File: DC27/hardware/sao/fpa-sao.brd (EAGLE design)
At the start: 160 x 100 mm, 45 parts, among them IC1 LDL112D33R, U1 ICE40UL1K-SWG16ITR1K, U2 MIC5504-1.2YM5-TR, U3 W25X20CLSNIG

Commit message: checking in sao changes
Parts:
- removed IC1: LDL112D33R, voltage-regulator:SOIC127P600X175-8N
- removed LED2, LED6, LED7, LED8: (no value), leds:LED3MM
- removed R10, R11, R5, R6, R7, R8, R9: (no value), passives:0805
- removed R4: 10 K, passives:0805
- removed U$12, U$13, U$14, U$15, U$16, U$17, U$18, U$19: APA1025050, leds:APA102_5050
- removed U1: ICE40UL1K-SWG16ITR1K, FPGA:BGA16N35P4X4_140X140X49N
- added C16: 15 pF, passives:C0805
- added C5: 0.1 uF, passives:C0805
- added J1: (no value), connector:1X06
- added J2: FPGA_PROG, connector:2X5_NOSILK
- added J3, J4: (no value), connector:1X18
- added LED1: (no value), leds:LED3MM
- added R2: 56 R, passives:1206
- added R3: 10 K, passives:0805
- added S1, S2: (no value), switches:SWITCH-SPDT_KIT
- added U$1: DC-27-SAO, defcon:3X2
- added U$10, U$6, U$7, U$8, U$9: APA1025050, leds:APA102_5050
- added U4: MIC5504-3.3YM5-TR, voltage-regulator:SOT23-5P95_280X145XL45X37N
- added U5: ICE5LP1K-SG48ITR, FPGA:QFN50P700X700X100-49N
- C10, C11, C12, C13: value 15 pF -> 0.1 uF
- C4: value 1 uF -> 0.1 uF
- moved R12 103.4 mm to (40.3, 89.0), turned to 180 degrees
- moved R13 99.1 mm to (29.2, 85.9), turned to 270 degrees
- moved U3 96.0 mm to (35.5, 85.6), turned to 180 degrees
- moved C15 95.2 mm to (24.6, 84.9)
- moved C4 70.5 mm to (-11.9, 2.45)
- moved C13 66.9 mm to (-32.9, 2.45)
- moved C12 56.1 mm to (-28.7, 2.45)
- moved LED3 52.0 mm to (39.8, 77.8), turned to 180 degrees
- moved C1 43.2 mm to (12.7, 97.8)
- moved LED4 42.8 mm to (39.8, 72.3), turned to 180 degrees
- moved C11 42.3 mm to (-24.5, 2.45)
- moved C2 41.6 mm to (15.9, 91.6), turned to 90 degrees
- moved LED5 32.2 mm to (40.1, 66.9), turned to 180 degrees
- moved C3 30.1 mm to (12.1, 85.7)
- moved U2 29.6 mm to (12.7, 88.9), turned to 270 degrees
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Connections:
- removed net BARCODE: R10.2, U1.A2
- removed net CDONE: R5.2, U1.C3
- removed net FLASH_CS: R4.1, U1.D1, U3.1
- removed net IRLED: R9.2, U1.A1
- removed net N$10: U$14.3, U$17.4
- removed net N$12: LED4.A, R7.1
- removed net N$13: LED3.A, R6.1
- removed net N$14: LED2.A, R5.1
- removed net N$24: U$12.3, U$13.4
- removed net N$25: U$12.2, U$13.5
- removed net N$26: U$15.4, U$16.3
- removed net N$27: U$15.5, U$16.2
- removed net N$28: U$14.4, U$15.3
- removed net N$29: U$14.5, U$15.2
- removed net N$30: U$13.2, U$16.5
- removed net N$31: U$13.3, U$16.4
- removed net N$32: U$17.2, U$18.5
- removed net N$33: U$17.3, U$18.4
- removed net N$34: U$18.3, U$19.4
- removed net N$35: U$18.2, U$19.5
- removed net N$37: U$14.2, U$17.5
- removed net N$9: LED5.A, R8.1
- removed net VCC3.3: R1.2
- removed net VCC5V: C4.2, IC1.4, IC1.5
- new net INIT: J2.8
- new net N$15: U$10.5, U$8.2
- new net N$17: U$10.4, U$8.3
- new net N$18: U$10.3, U$11.4
- new net N$19: U$10.2, U$11.5
- new net N$2: R2.2, U5.7
- new net N$21: U$11.2, U$9.5
- new net N$22: U$11.3, U$9.4
- new net N$3: R1.1, U5.8
- new net N$5: U$6.2, U$7.5
- new net PROG_FLASH_CS: J1.5, S1.3
- new net SAO_VCC_IN: C1.1, J2.6, U$1.1, U4.1, U4.3
- new net SCL: U$1.5, U5.18
- new net SDA: U$1.2, U5.19
- new net SPI_CS: R3.2, S1.1, U5.16
- new net SPI_MEM_CS: S1.2, U3.1
- new net TRST: J2.9
- net GND: now also C10.1, C11.1, C12.1, C13.1, C16.2, C5.1, J1.6, J2.2, J2.4, J3.1, J4.18, LED1.K, S2.1, U$1.4, U$10.6, U$6.6, U$7.6, U$8.6, U$9.6, U4.2, U5.49; no longer C10.2, C11.2, C12.2, C13.2, IC1.2, IC1.3, IC1.6, IC1.7, LED2.K, LED3.K, LED4.K, LED5.K, LED6.K, LED7.K, LED8.K, U$12.6, U$13.6, U$14.6, U$15.6, U$16.6, U$17.6, U$18.6, U$19.6, U1.A3, U1.B1
- net MISO: now also J1.4, J2.5, U5.14; no longer R11.2, U1.C2
- net MOSI: now also J1.3, J2.7, U$6.4, U5.17; no longer U$11.4, U1.D2
- net N$1: now also LED1.A, R2.1; no longer U$11.2, U$12.5
- net N$23: now also J2.3; no longer U$11.3, U$12.4
- net N$4: now also R3.1, S2.2; no longer R1.1, U1.B2
- net N$6: now also U$6.3, U$7.4; no longer LED8.A, R11.1
- net N$7: now also U$7.3, U$8.4; no longer LED7.A, R10.1
- net N$8: now also U$7.2, U$8.5; no longer LED6.A, R9.1
- net RGB0: now also LED3.K, U5.41; no longer R6.2, U1.B4
- net RGB1: now also LED4.K, U5.40; no longer R7.2, U1.A4
- net RGB2: now also LED5.K, U5.39; no longer R8.2, U1.C4
- net SCK: now also J1.2, J2.1, U$6.5, U5.15; no longer U$11.5, U1.C1
- net VCC1.2V: now also C12.2, C13.2, J4.1, U5.29, U5.30, U5.5; no longer U1.D4
- net VCC3.3V: now also C10.2, C11.2, C16.1, C4.2, C5.2, J1.1, J3.18, LED3.A, LED4.A, LED5.A, R1.2, S2.3, U$10.1, U$6.1, U$7.1, U$8.1, U4.5, U5.1, U5.22, U5.24, U5.33; no longer C1.1, C10.1, C11.1, C12.1, C13.1, IC1.1, R4.2, U$12.1, U$13.1, U$14.1, U$15.1, U$16.1, U$17.1, U$18.1, U$19.1, U1.B3, U1.D3
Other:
- board size 160 x 100 mm -> 43.2 x 100 mm

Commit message: updated sao
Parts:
- removed U$11, U$9: APA1025050, leds:APA102_5050
- added C17, C18: 15 pF, passives:C0805
- added U$2, U$3, U$4, U$5: APA1025050, leds:APA102_5050
- moved C7 79.6 mm to (-32.9, -18.2)
- moved C14 69.3 mm to (-28.7, -18.2)
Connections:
- removed net N$18: U$10.3, U$11.4
- removed net N$19: U$10.2, U$11.5
- removed net N$21: U$11.2, U$9.5
- removed net N$22: U$11.3, U$9.4
- new net MOSI-2: U$2.4, U5.23
- new net N$12: U$2.3, U$3.4
- new net N$13: U$3.3, U$4.4
- new net N$14: U$3.2, U$4.5
- new net N$15: U$4.3, U$5.4
- new net N$17: U$4.2, U$5.5
- new net N$9: U$2.2, U$3.5
- new net SCK-2: U$2.5, U5.26
- net GND: now also C17.2, C18.2, U$2.6, U$3.6, U$4.6, U$5.6; no longer U$11.6, U$9.6
- net VCC3.3V: now also C17.1, C18.1, U$2.1, U$3.1, U$4.1, U$5.1; no longer U$11.1

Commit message: updated sao and docs
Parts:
- added J5: (no value), connector:1X06
- moved U$5 65.3 mm to (33.2, 18.0)
- moved U$4 63.1 mm to (24.4, 18.0)
- moved U$3 47.1 mm to (16.7, 18.4)
- moved U$2 46.0 mm to (9.14, 18.4)
- moved U$10 12.9 mm to (5.40, 26.2), turned to 180 degrees
- moved U5 10.2 mm to (22.1, 67.2), turned to 180 degrees
- moved J2 1.27 mm to (23.1, 3.98)
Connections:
- removed net N$3: R1.1, U5.8
- new net 0A: J3.13, U5.46
- new net 16A: J3.8, U5.9
- new net 18A: J3.7, U5.10
- new net 20A: J3.6, U5.11
- new net 22A: J3.5, U5.12
- new net 23B: J4.17, U5.21
- new net 24A: J3.4, U5.13
- new net 25B: J3.15, U5.20
- new net 2A: J3.12, U5.47
- new net 36B: J4.8, U5.25
- new net 38B: J4.9, U5.27
- new net 3B: J3.14, U5.44
- new net 41A: J4.4, U5.28
- new net 42B: J4.10, U5.31
- new net 43A: J4.5, U5.32
- new net 44B: J4.11, U5.34
- new net 45A: J3.16, U5.37
- new net 46B: J3.17, U5.35
- new net 48B: J4.12, U5.36
- new net 49A: J4.6, U5.43
- new net 4A: J3.11, U5.48
- new net 50B: J4.13, U5.38
- new net 51A: J4.7, U5.42
- new net 5B: J3.3, U5.45
- new net 6A: J3.10, U5.2
- new net 8A: J3.9, U5.4
- new net 9B: J3.2, U5.3
- new net CRESET: R1.1, U5.6, U5.8
- net GND: now also J5.1
- net MOSI-2: now also J4.2
- net RGB0: now also J4.14
- net RGB1: now also J4.15
- net RGB2: now also J4.16
- net SAO_VCC_IN: now also J5.2
- net SCK-2: now also J4.3
- net SCL: now also J5.4
- net SDA: now also J5.5
- net VCC1.2V: now also J5.3
- net VCC3.3V: now also J5.6

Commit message: tied pin 6 to cdone
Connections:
- new net CDONE: U5.6
- net CRESET: no longer U5.6
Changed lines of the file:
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@@
 <contactref element="U5" pad="8"/>
 <contactref element="R1" pad="1"/>
-<contactref element="U5" pad="6"/>
 <wire x1="25.485" y1="67.95" x2="20.65" y2="82.75" width="0" layer="19" extent="1-1"/>
-<wire x1="25.485" y1="66.95" x2="25.485" y2="67.95" width="0" layer="19" extent="1-1"/>
 </signal>
 <signal name="PROG_FLASH_CS">
@@
 <wire x1="3.15" y1="67.93" x2="19.8" y2="63.765" width="0" layer="19" extent="1-1"/>
 </signal>
+<signal name="CDONE">
+<contactref element="U5" pad="6"/>
+</signal>
 </signals>

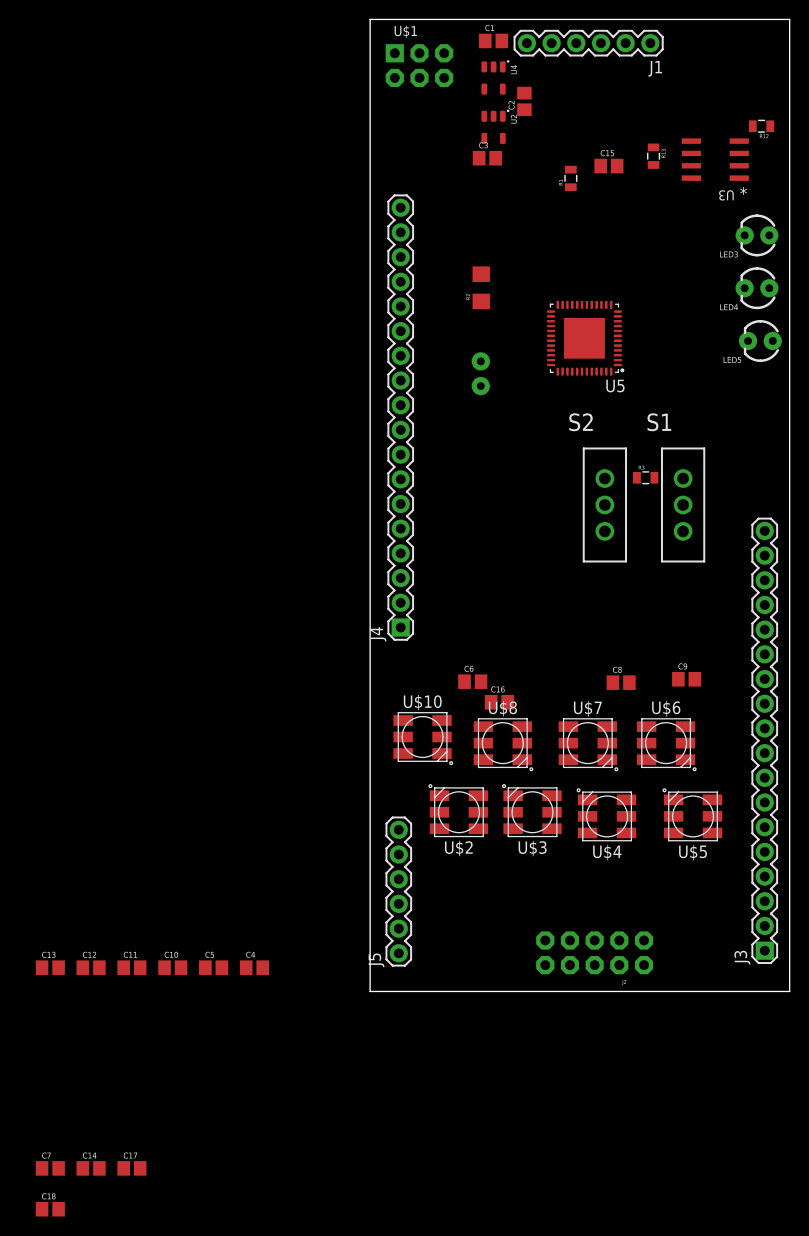
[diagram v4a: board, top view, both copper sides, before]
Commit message: final tweaks moved top board I2C to separate bus
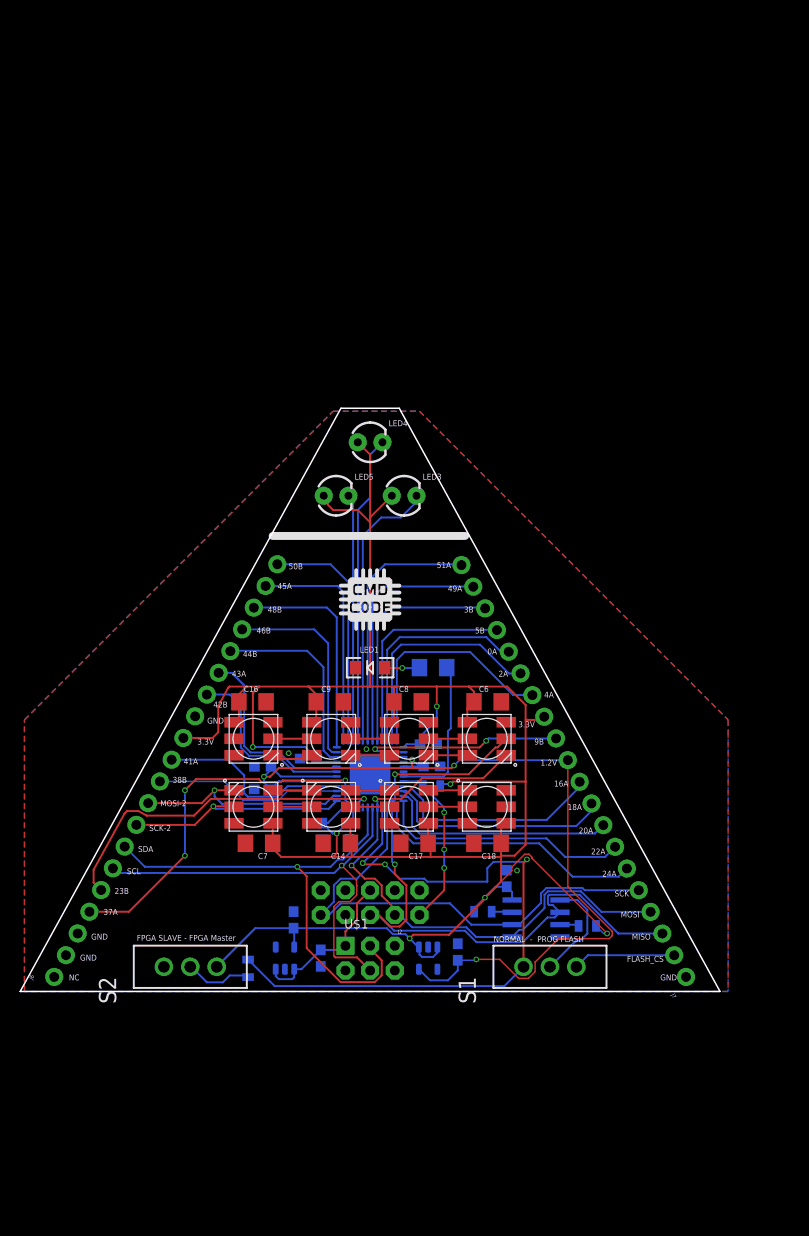
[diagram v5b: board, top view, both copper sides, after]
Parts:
- removed J1, J5: (no value), connector:1X06
- removed J3, J4: (no value), connector:1X18
- added C19: 0.1 uF, passives:C0603
- added J6, J7: (no value), connector:1X20_NO_SILK_KIT
- added U$9: CMD_C0DE_LOGOCMD_CODE_LOGO_SILK, logos:CMD_C0DE_LOGO_SILK
- C1, C10, C11, C12, C13, C15, C2, C3, C4, C5: device passives:C0805 -> passives:C0603
- C14, C16, C17, C18, C6, C7, C8, C9: device passives:C0805 -> passives:C1206
- LED1: device leds:LED3MM -> leds:LED-1206
- moved C1 96.0 mm to (-5.08, 3.43), flipped to the bottom, turned to 270 degrees
- moved U4 93.1 mm to (-8.76, 3.43), flipped to the bottom, turned to 90 degrees
- moved U$1 92.0 mm to (0.00, 3.43)
- moved C2 87.5 mm to (-7.87, 7.37), flipped to the bottom
- moved U2 85.7 mm to (5.97, 3.43), flipped to the bottom
- moved R12 84.2 mm to (22.3, 6.74), flipped to the bottom, turned to 0 degrees
- moved C3 81.7 mm to (9.02, 4.06), flipped to the bottom, turned to 270 degrees
- moved U3 80.2 mm to (17.1, 7.51), flipped to the bottom, turned to 0 degrees
- moved R13 79.7 mm to (11.6, 8.21), flipped to the bottom, turned to 180 degrees
- moved C15 74.0 mm to (14.1, 11.6), flipped to the bottom, turned to 90 degrees
- moved R3 65.0 mm to (-12.6, 2.38), flipped to the bottom, turned to 90 degrees
- moved R1 64.1 mm to (6.31, 21.1), flipped to the bottom, turned to 180 degrees
- moved S2 63.8 mm to (-18.5, 2.54), turned to 90 degrees
- moved C18 58.7 mm to (12.1, 15.2), turned to 180 degrees
- moved U5 50.0 mm to (0.00, 22.4), flipped to the bottom, turned to 0 degrees
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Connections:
- removed net 25B: J3.15, U5.20
- removed net 36B: J4.8, U5.25
- removed net 6A: J3.10, U5.2
- removed net 8A: J3.9, U5.4
- removed net N$2: R2.2, U5.7
- removed net N$23: J2.3
- removed net TRST: J2.9
- new net 37A: J6.4, U5.23
- net 0A: now also J7.16; no longer J3.13
- net 16A: now also J7.10; no longer J3.8
- net 18A: now also J7.9; no longer J3.7
- net 20A: now also J7.8; no longer J3.6
- net 22A: now also J7.7; no longer J3.5
- net 23B: now also J6.5; no longer J4.17
- net 24A: now also J7.6; no longer J3.4
- net 2A: now also J7.15; no longer J3.12
- net 38B: now also J6.10; no longer J4.9
- net 3B: now also J7.18; no longer J3.14
- net 41A: now also J6.11; no longer J4.4
- net 42B: now also J6.14; no longer J4.10
- net 43A: now also J6.15; no longer J4.5
- net 44B: now also J6.16; no longer J4.11
- net 45A: now also J6.19; no longer J3.16
- net 46B: now also J6.17; no longer J3.17
- net 48B: now also J6.18; no longer J4.12
- net 49A: now also J7.19; no longer J4.6
- net 4A: now also J7.14; no longer J3.11
- net 50B: now also J6.20; no longer J4.13
- net 51A: now also J7.20; no longer J4.7
- net 5B: now also J7.17; no longer J3.3
- net 9B: now also J7.12; no longer J3.2
- net CDONE: now also R2.2, U5.7
- net CRESET: now also J2.9
- net GND: now also C19.1, J6.13, J6.2, J6.3, J7.1, LED1.C; no longer J1.6, J3.1, J4.18, J5.1, LED1.K
- net MISO: now also J7.3; no longer J1.4
- net MOSI: now also J7.4; no longer J1.3
- net MOSI-2: now also J6.9, U5.26; no longer J4.2, U5.23
- net PROG_FLASH_CS: now also J7.2; no longer J1.5
- net RGB0: no longer J4.14
- net RGB1: no longer J4.15
- net RGB2: no longer J4.16
- net SAO_VCC_IN: no longer J5.2
- net SCK: now also J7.5; no longer J1.2
- net SCK-2: now also J6.8, U5.25; no longer J4.3, U5.26
- net SCL: now also J6.6; no longer J5.4
- net SDA: now also J6.7; no longer J5.5
- net VCC1.2V: now also C19.2, C5.2, J7.11; no longer C12.2, J4.1, J5.3
- net VCC3.3V: now also C12.2, J6.12, J7.13; no longer C5.2, J1.1, J3.18, J5.6
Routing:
- net VCC3.3V: track 0.00 -> 261.2 mm, vias 0 -> 7
- net VCC1.2V: track 0.00 -> 98.8 mm, vias 0 -> 4
- net SCK: track 0.00 -> 68.2 mm, vias 0 -> 1
- net SPI_CS: track 0.00 -> 67.5 mm, vias 0 -> 3
- net MOSI: track 0.00 -> 61.8 mm, vias 0 -> 2
- net MISO: track 0.00 -> 54.5 mm, vias 0 -> 1
- net SDA: track 0.00 -> 51.8 mm, vias 0 -> 1
- net SCL: track 0.00 -> 47.4 mm, vias 0 -> 1
- net 37A: track 0.00 -> 39.0 mm, vias 0 -> 3
- net 23B: track 0.00 -> 35.9 mm, vias 0 -> 1
- net RGB1: track 0.00 -> 31.8 mm
- net RGB0: track 0.00 -> 28.7 mm
- net 24A: track 0.00 -> 28.1 mm
- net 51A: track 0.00 -> 26.8 mm
- net 22A: track 0.00 -> 26.1 mm
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- added copper zone on layer 1, net GND
- added copper zone on layer 16, net GND
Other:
- board size 43.2 x 100 mm -> 72 x 60 mm
- board text added: "0A"
- board text added: "1.2V"
- board text added: "16A"
- board text added: "18A"
- board text added: "20A"
- board text added: "22A"
- board text added: "23B"
- board text added: "24A"
- board text added: "2A"
- board text added: "3.3V"
- board text added: "37A"
- board text added: "38B"
- board text added: "3B"
- board text added: "41A"
- board text added: "42B"
- board text added: "43A"
- board text added: "44B"
- board text added: "45A"
- board text added: "46B"
- board text added: "48B"
- board text added: "49A"
- board text added: "4A"
- board text added: "50B"
- board text added: "51A"
- board text added: "5B"
- board text added: "9B"
- board text added: "FLASH_CS"
- board text added: "FPGA SLAVE - FPGA Master"
- board text added: "GND"
- board text added: "MISO"
- board text added: "MOSI"
- board text added: "MOSI-2"
- board text added: "NC"
- board text added: "NORMAL - PROG FLASH"
- board text added: "SCK"
- board text added: "SCK-2"
- board text added: "SCL"
- board text added: "SDA"
